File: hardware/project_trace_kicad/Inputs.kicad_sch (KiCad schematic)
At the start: 50 parts, among them J201 Conn_01x01_Socket, J202 Conn_01x01_Socket, J203 Conn_01x01_Socket, J204 Screw_Terminal_01x04, J205 Conn_Coaxial, U201 TLE2426xLP, U202 AQW280SX, U203 AQW282SX, U204 OPA2837IRUNT, U205 TS5A23159DGS, U206 OPA2837IRUNT, U207 SN74LVC2G14DBV

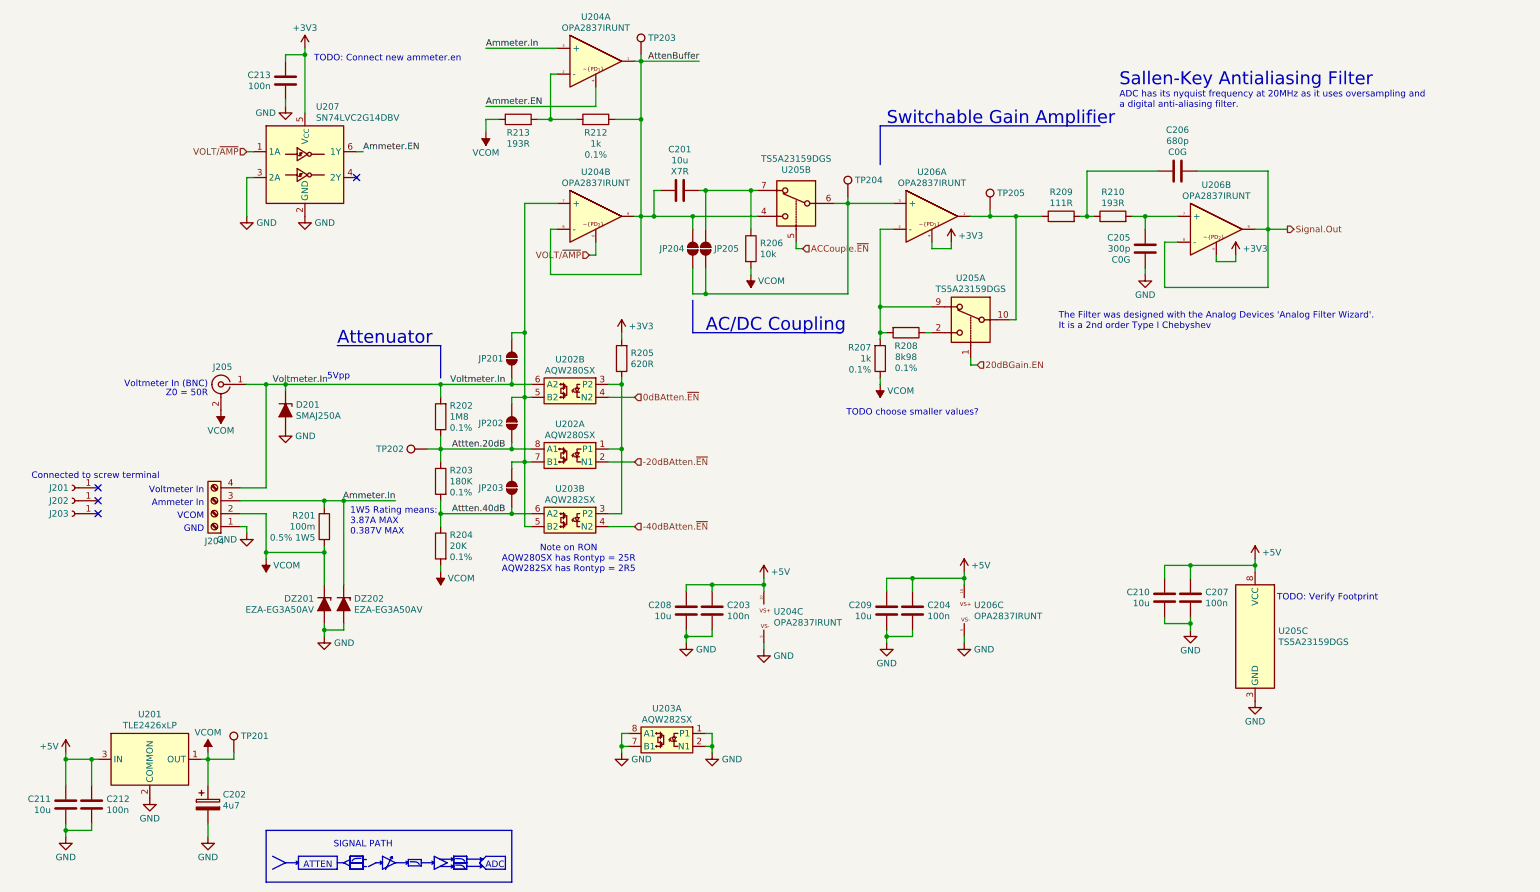
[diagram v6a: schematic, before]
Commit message: ERC Checks & Bug-Fixing
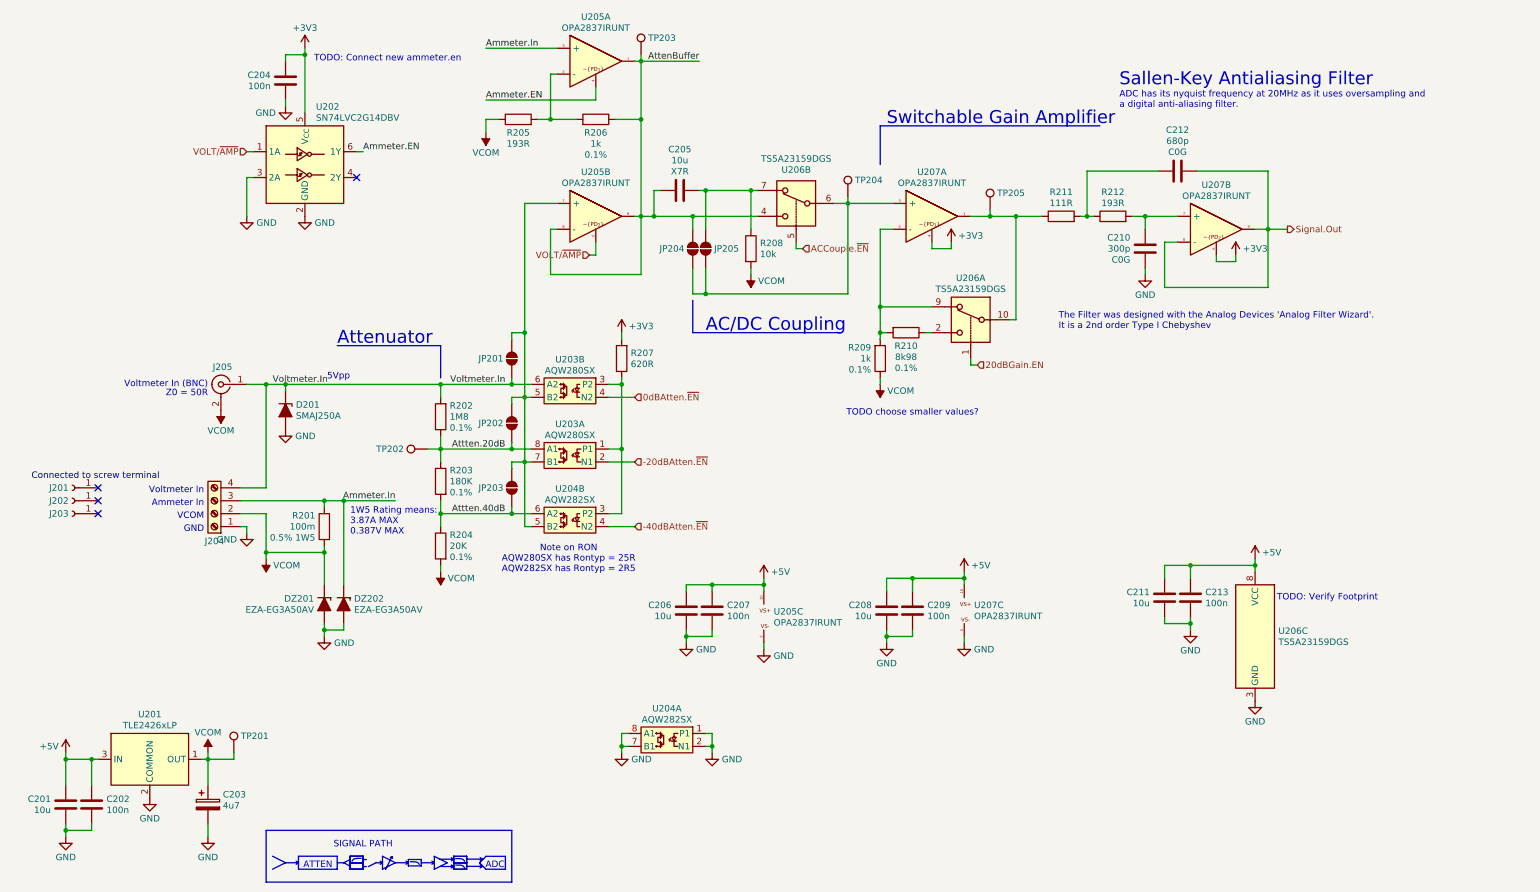
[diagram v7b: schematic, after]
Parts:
- U206: renamed from U205; footprint ProjectTraceFootprints:SOIC-10 - DGS0010A -> Package_SO:TSSOP-10_3x3mm_P0.5mm
- renumbered C211 to C201, C212 to C202, C202 to C203, C213 to C204, C201 to C205, C208 to C206, C203 to C207, C209 to C208, C204 to C209, C205 to C210, C210 to C211, C206 to C212, C207 to C213, R213 to R205, R212 to R206, R205 to R207, R206 to R208, R207 to R209, R208 to R210, R209 to R211, R210 to R212, U207 to U202, U202 to U203, U203 to U204, U204 to U205, U206 to U207

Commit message: Partnumbers and BOM updated
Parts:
- J201, J202, J203: DigikeyPN 4654-FCR144635-ND -> (none)
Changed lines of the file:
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@@
-			)
-		)
-		(property "DigikeyPN" "4654-FCR144635-ND"
-			(at 21.59 116.84 0)
-			(hide yes)
-			(show_name no)
-			(do_not_autoplace no)
-			(effects
-				(font
-					(size 1.27 1.27)
-				)
 			)
 		)
@@
 			)
 		)
-		(property "DigikeyPN" "4654-FCR144635-ND"
-			(at 21.59 119.38 0)
-			(hide yes)
-			(show_name no)
-			(do_not_autoplace no)
-			(effects
-				(font
-					(size 1.27 1.27)
-				)
-			)
-		)
 		(pin "1"
 		)
@@
 			(at 21.59 121.92 0)
 			(hide yes)
-			(show_name no)
-			(do_not_autoplace no)
-			(effects
-				(font
-					(size 1.27 1.27)
-				)
-			)
-		)
-		(property "DigikeyPN" "4654-FCR144635-ND"
-			(at 21.59 121.92 0)
-			(hide yes)
